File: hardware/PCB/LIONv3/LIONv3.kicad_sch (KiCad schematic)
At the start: 35 parts, among them J1 CAN, J2 UART, J3 JTAG, J4 PWR_GND, J5 PWR_3.3V, J6 PWR_5V, J7 I2C, SW1 RESET, SW2 BOOT, U12 TYPE-C_16PIN_2MD(073), U2 ESP32-C6-MINI-1-N4, U5 TCAN3414DR, U6 TMP112AIDRLR

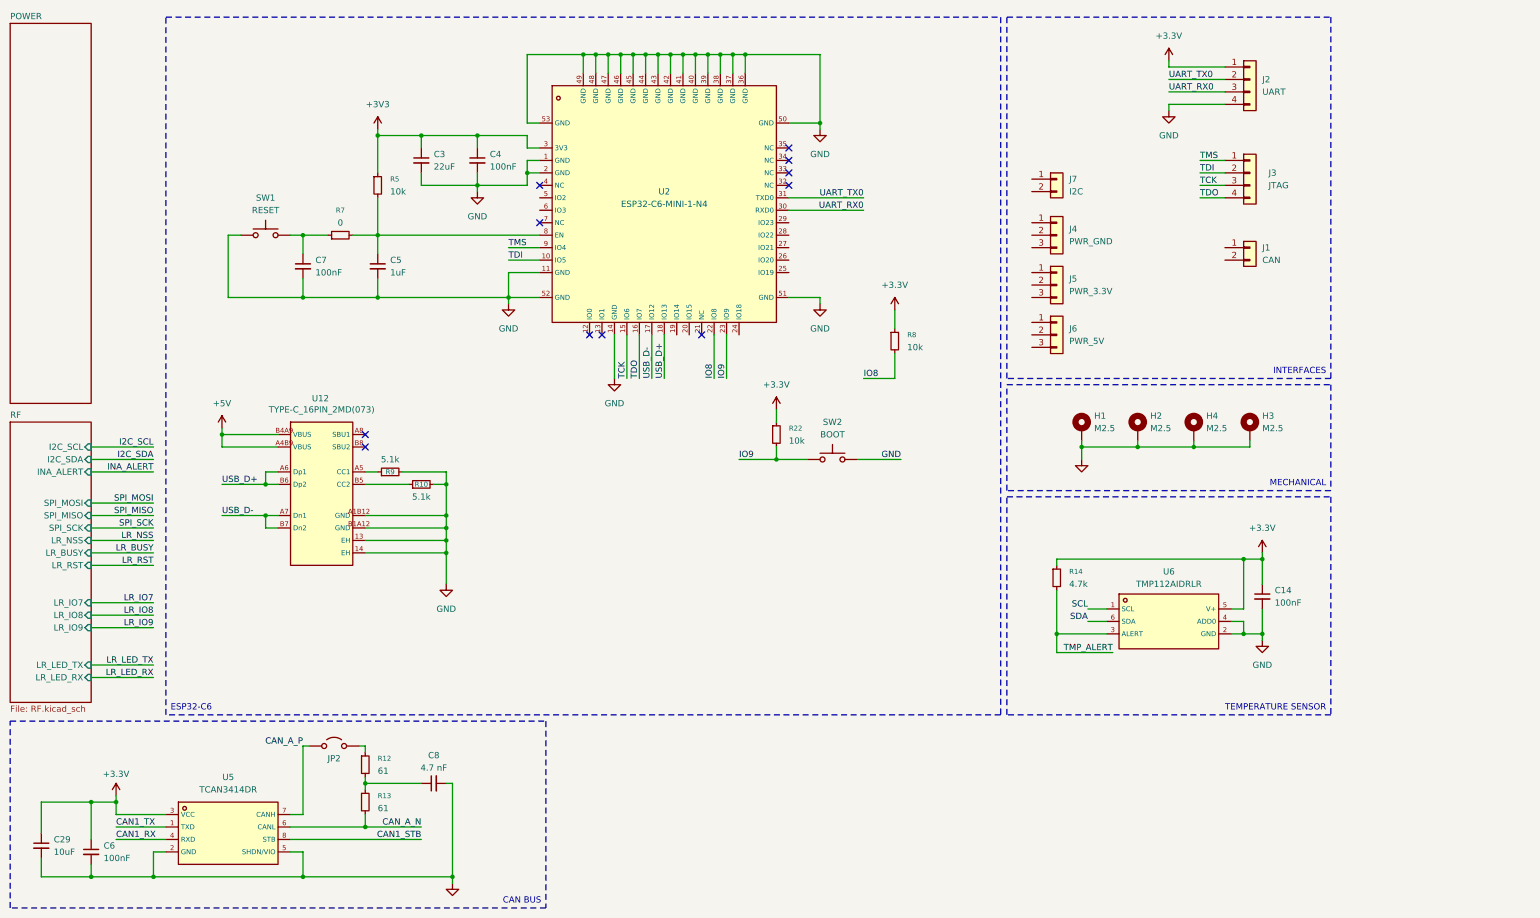
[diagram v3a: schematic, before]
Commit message: feat(hardware): add MOLEX connectors
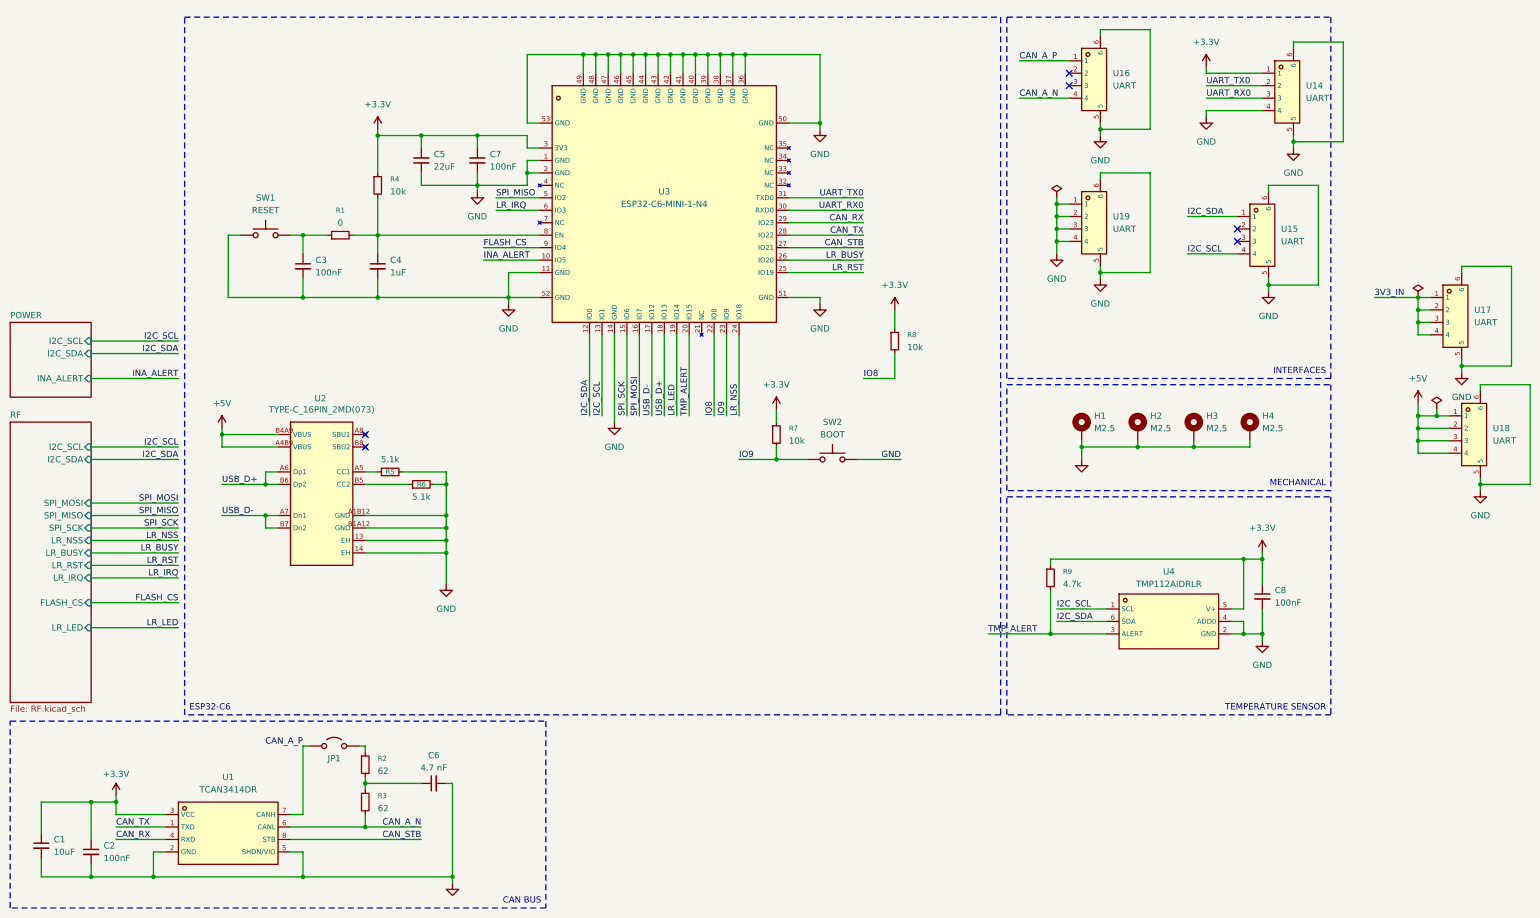
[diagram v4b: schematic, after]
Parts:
- removed J1: CAN, Connector_Molex:Molex_PicoBlade_53048-0210_1x02_P1.25mm_Horizontal, symbol Connector_Generic:Conn_01x02
- removed J2: UART, Connector_Molex:Molex_PicoBlade_53048-0410_1x04_P1.25mm_Horizontal, symbol Connector_Generic:Conn_01x04
- removed J3: JTAG, Connector_Molex:Molex_PicoBlade_53048-0410_1x04_P1.25mm_Horizontal, symbol Connector_Generic:Conn_01x04
- removed J4: PWR_GND, Connector_Molex:Molex_PicoBlade_53048-0310_1x03_P1.25mm_Horizontal, symbol Connector_Generic:Conn_01x03
- removed J5: PWR_3.3V, Connector_Molex:Molex_PicoBlade_53048-0310_1x03_P1.25mm_Horizontal, symbol Connector_Generic:Conn_01x03
- removed J6: PWR_5V, Connector_Molex:Molex_PicoBlade_53048-0310_1x03_P1.25mm_Horizontal, symbol Connector_Generic:Conn_01x03
- removed J7: I2C, Connector_Molex:Molex_PicoBlade_53048-0210_1x02_P1.25mm_Horizontal, symbol Connector_Generic:Conn_01x02
- removed R14: 4.7k, Resistor_SMD:R_0402_1005Metric, symbol Device:R_Small
- added R9: 4.7k, Resistor_SMD:R_0402_1005Metric, symbol Device:R_Small
- added U14, U15, U16, U17, U18, U19: UART, LIONv3-Footprints:CONN-SMD_4P-P1.25_53261-0471, symbol LIONv3-Symbols:532610471_C696092
- C1: renamed from C29; LCSC (none) -> C440198
- C2: renamed from C6; LCSC (none) -> C307331
- C3: renamed from C7; LCSC (none) -> C307331
- C4: renamed from C5; LCSC (none) -> C15849
- C5: renamed from C3; LCSC (none) -> C45783
- C6: renamed from C8; LCSC (none) -> C1518204
- C7: renamed from C4; LCSC (none) -> C307331
- C8: renamed from C14; LCSC (none) -> C307331
- R1: renamed from R7; LCSC (none) -> C17168
- R2: renamed from R12; value 61 -> 62; LCSC (none) -> C2909376
- R3: renamed from R13; value 61 -> 62; LCSC (none) -> C2909376
- R4: renamed from R5; LCSC (none) -> C25744
- R5: renamed from R9; LCSC (none) -> C25905
- R6: renamed from R10; LCSC (none) -> C25905
- R7: renamed from R22; footprint (none) -> Resistor_SMD:R_0402_1005Metric; LCSC (none) -> C25744
- SW1, SW2: footprint (none) -> LIONv3-Footprints:KEY-SMD_L3.9-W3.0-LS5.0; LCSC (none) -> C5373431
- U1: renamed from U5; symbol TET-Symbols:TCAN3414DR -> LIONv3-Symbols:TCAN3414DR
- U4: renamed from U6; symbol TET-Symbols:TMP112AIDRLR -> LIONv3-Symbols:TMP112AIDRLR
- renumbered H4 to H3, H3 to H4, JP2 to JP1, U12 to U2, U2 to U3
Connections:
- net +3V3 is gone; now on net +3.3V: C5.1, C7.1, R4.1, U3.3 (3V3)
- net CAN1_RX is gone; now on net CAN_RX: U1.4 (RXD)
- net CAN1_STB is gone; now on net CAN_STB: U1.8 (STB)
- net CAN1_TX is gone; now on net CAN_TX: U1.1 (TXD)
- net SCL is gone; now on net I2C_SCL: U4.1 (SCL)
- net SDA is gone; now on net I2C_SDA: U4.6 (SDA)
- net TCK is gone; now on net SPI_SCK: U3.15 (IO6)
- net TDI is gone; now on net INA_ALERT: U3.10 (IO5)
- net TDO is gone; now on net SPI_MOSI: U3.16 (IO7)
- net +3.3V: now also R9.1, U14.1
- net +5V: now also U18.1, U18.2, U18.3, U18.4
- net CAN_A_N: now also U16.4
- net CAN_A_P: now also U16.1
- net GND: now also U14.4, U14.5, U14.6, U15.5, U15.6, U16.5, U16.6, U17.5, U17.6, U18.5, U18.6, U19.1, U19.2, U19.3, U19.4, U19.5, U19.6
- net I2C_SCL: now also U3.13 (IO1), U15.4
- net I2C_SDA: now also U3.12 (IO0), U15.1
- net LR_BUSY: now also U3.26 (IO20)
- net LR_NSS: now also U3.24 (IO18)
- net LR_RST: now also U3.25 (IO19)
- net SPI_MISO: now also U3.5 (IO2)
- net TMP_ALERT: now also U3.20 (IO15), R9.2
- net UART_RX0: now also U14.3
- net UART_TX0: now also U14.2
- net LR_LED: now reaches U3.19 (IO14)
- net CAN_STB: now reaches U3.27 (IO21)
- net CAN_TX: now reaches U3.28 (IO22)
- net CAN_RX: now reaches U3.29 (IO23)
- net LR_IRQ: now reaches U3.6 (IO3)
- net TMS renamed FLASH_CS
- new net 3V3_IN: U17.1, U17.2, U17.3, U17.4
- no-connect marks 11 -> 6
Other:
- sheet POWER ports: added I2C_SCL, I2C_SDA, INA_ALERT; removed none
- sheet RF ports: added FLASH_CS, LR_IRQ, LR_LED; removed INA_ALERT, LR_IO7, LR_IO8, LR_IO9, LR_LED_RX, LR_LED_TX

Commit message: feat(hardware): finish board schematic
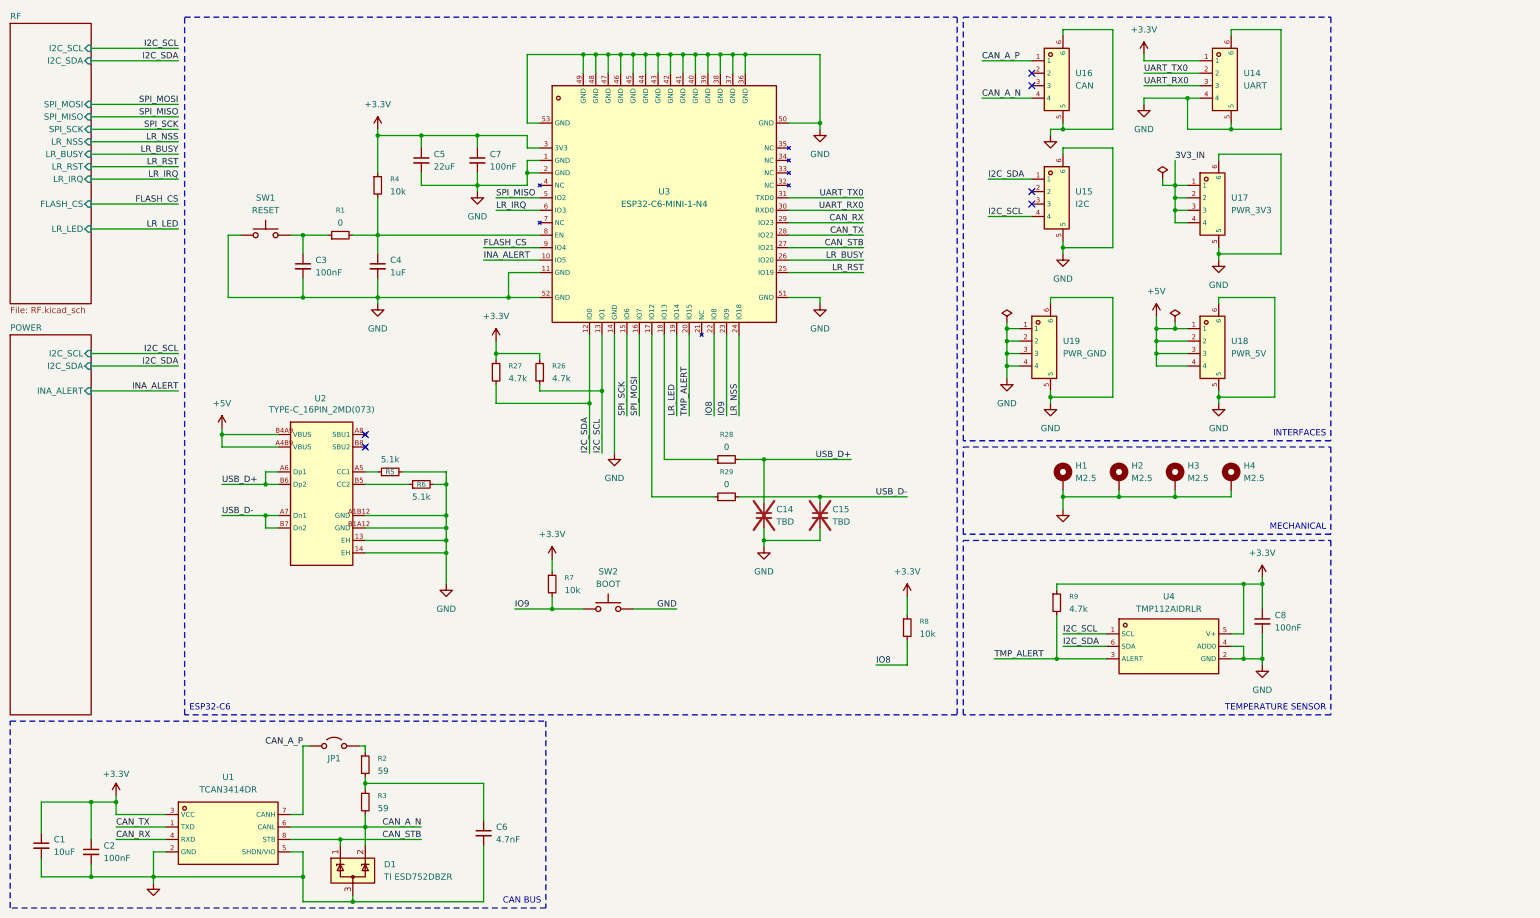
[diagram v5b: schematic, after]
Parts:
- added C14, C15: TBD, Capacitor_SMD:C_0402_1005Metric, symbol Device:C_Small
- added D1: TI ESD752DBZR, Package_TO_SOT_SMD:SOT-23-3, symbol Power_Protection:ESDA5V3L
- added R26, R27: 4.7k, Resistor_SMD:R_0402_1005Metric, symbol Device:R_Small
- added R28, R29: 0, Resistor_SMD:R_0402_1005Metric, symbol Device:R_Small
- C6: value 4.7 nF -> 4.7nF; LCSC C1518204 -> C1538
- R2, R3: value 62 -> 59; LCSC C2909376 -> C2998103
- R8: LCSC (none) -> C25744
- U15: value UART -> I2C
- U16: value UART -> CAN
- U17: value UART -> PWR_3V3
- U18: value UART -> PWR_5V
- U19: value UART -> PWR_GND
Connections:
- net +3.3V: now also R26.2, R27.1
- net CAN_A_N: now also D1.2 (K)
- net CAN_STB: now also D1.1 (K)
- net GND: now also C14.2, C15.2, D1.3 (A)
- net I2C_SCL: now also R26.1
- net I2C_SDA: now also R27.2
- net USB_D+: now also C14.1, R28.2; no longer U3.18 (IO13)
- net USB_D-: now also C15.1, R29.2; no longer U3.17 (IO12)
- new net: R29.1, U3.17 (IO12)
- new net: R28.1, U3.18 (IO13)
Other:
- moved on the sheet: C8, H1, H2, H3, H4, R7, R8, R9, SW2, U14, U15, U16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
